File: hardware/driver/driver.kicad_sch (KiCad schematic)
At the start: 71 parts, among them J1 BTB 30P socket, J2 BTB 30P socket, J3 BTB 30P header, J4 BTB 30P header, U1 AT8833CQ, U10 AT8833CQ, U2 AT8833CQ, U3 AT8833CQ, U4 AT8833CQ, U5 AT8833CQ, U6 AT8833CQ, U7 AT8833CQ, U8 AT8833CQ, U9 AT8833CQ

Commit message: Schematic review fixes from datasheet checks
- Crystal: Abracon ABM8-272-T3, which the RP2350 design guide's
  15 pF / 1k values are tuned for (the YXC part needs 20 pF load).
- Status LED: power from V5 and buffer the 3.3 V data through a
  74AHCT1G125; the diode drop left VDD below the 3.7 V minimum.
- Qwiic: drop the BAT54WS power-in path. The ME6211 conducts from
  VOUT to VIN, so a Qwiic-fed 3V3 would back-power V5.
- Notes: sense resistors chop at 0.2-0.29 A rather than fault;
  the NO_ESTOP jumper must be cut when an e-stop is fitted.
- README: AT8833 capacitor values, inductor orientation, VMOT_SENSE
  limits, and open items (V5 capacitance, e-stop masking by a held
  button, E9 reset behaviour on motor inputs).

Co-Authored-By: Claude Opus 5.5 <noreply@anthropic.com>
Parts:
- R1, R10, R11, R12, R13, R14, R15, R16, R17, R18, R19, R2, R20, R3, R4, R5, R6, R7, R8, R9: Note current cap ~0.2-0.29 A; Kelvin return -> chops at 0.2-0.29 A (VTRIP 160-240 mV); Kelvin return
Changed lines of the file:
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@@
 			)
 		)
-		(property "Note" "current cap ~0.2-0.29 A; Kelvin return"
+		(property "Note" "chops at 0.2-0.29 A (VTRIP 160-240 mV); Kelvin return"
 			(at 116.84 40.64 0)
 			(hide yes)
@@
 			)
 		)
-		(property "Note" "current cap ~0.2-0.29 A; Kelvin return"
+		(property "Note" "chops at 0.2-0.29 A (VTRIP 160-240 mV); Kelvin return"
 			(at 167.64 40.64 0)
 			(hide yes)
@@
 			)
 		)
-		(property "Note" "current cap ~0.2-0.29 A; Kelvin return"
+		(property "Note" "chops at 0.2-0.29 A (VTRIP 160-240 mV); Kelvin return"
 			(at 492.76 40.64 0)
 			(hide yes)
@@
 			)
 		)
-		(property "Note" "current cap ~0.2-0.29 A; Kelvin return"
+		(property "Note" "chops at 0.2-0.29 A (VTRIP 160-240 mV); Kelvin return"
 			(at 43.18 86.36 0)
 			(hide yes)
@@
 			)
 		)
-		(property "Note" "current cap ~0.2-0.29 A; Kelvin return"
+		(property "Note" "chops at 0.2-0.29 A (VTRIP 160-240 mV); Kelvin return"
 			(at 368.3 86.36 0)
 			(hide yes)
@@
 			)
 		)
-		(property "Note" "current cap ~0.2-0.29 A; Kelvin return"
+		(property "Note" "chops at 0.2-0.29 A (VTRIP 160-240 mV); Kelvin return"
 			(at 416.56 86.36 0)
 			(hide yes)
@@
 			)
 		)
-		(property "Note" "current cap ~0.2-0.29 A; Kelvin return"
+		(property "Note" "chops at 0.2-0.29 A (VTRIP 160-240 mV); Kelvin return"
 			(at 218.44 129.54 0)
 			(hide yes)
@@
 			)
 		)
-		(property "Note" "current cap ~0.2-0.29 A; Kelvin return"
+		(property "Note" "chops at 0.2-0.29 A (VTRIP 160-240 mV); Kelvin return"
 			(at 266.7 129.54 0)
 			(hide yes)
@@
 			)
 		)
-		(property "Note" "current cap ~0.2-0.29 A; Kelvin return"
+		(property "Note" "chops at 0.2-0.29 A (VTRIP 160-240 mV); Kelvin return"
 			(at 116.84 175.26 0)
 			(hide yes)
@@
 			)
 		)
-		(property "Note" "current cap ~0.2-0.29 A; Kelvin return"
+		(property "Note" "chops at 0.2-0.29 A (VTRIP 160-240 mV); Kelvin return"
 			(at 167.64 175.26 0)
 			(hide yes)
@@
 			)
 		)
-		(property "Note" "current cap ~0.2-0.29 A; Kelvin return"
+		(property "Note" "chops at 0.2-0.29 A (VTRIP 160-240 mV); Kelvin return"
 			(at 492.76 175.26 0)
 			(hide yes)
@@
 			)
 		)
-		(property "Note" "current cap ~0.2-0.29 A; Kelvin return"
+		(property "Note" "chops at 0.2-0.29 A (VTRIP 160-240 mV); Kelvin return"
 			(at 43.18 220.98 0)
 			(hide yes)
@@
 			)
 		)
-		(property "Note" "current cap ~0.2-0.29 A; Kelvin return"
+		(property "Note" "chops at 0.2-0.29 A (VTRIP 160-240 mV); Kelvin return"
 			(at 368.3 220.98 0)
 			(hide yes)
@@
 			)
 		)
-		(property "Note" "current cap ~0.2-0.29 A; Kelvin return"
+		(property "Note" "chops at 0.2-0.29 A (VTRIP 160-240 mV); Kelvin return"
 			(at 416.56 220.98 0)
 			(hide yes)
@@
 			)
 		)
-		(property "Note" "current cap ~0.2-0.29 A; Kelvin return"
+		(property "Note" "chops at 0.2-0.29 A (VTRIP 160-240 mV); Kelvin return"
 			(at 218.44 264.16 0)
 			(hide yes)
@@
 			)
 		)
-		(property "Note" "current cap ~0.2-0.29 A; Kelvin return"
+		(property "Note" "chops at 0.2-0.29 A (VTRIP 160-240 mV); Kelvin return"
 			(at 266.7 264.16 0)
 			(hide yes)
@@
 			)
 		)
-		(property "Note" "current cap ~0.2-0.29 A; Kelvin return"
+		(property "Note" "chops at 0.2-0.29 A (VTRIP 160-240 mV); Kelvin return"
 			(at 116.84 309.88 0)
 			(hide yes)
@@
 			)
 		)
-		(property "Note" "current cap ~0.2-0.29 A; Kelvin return"
+		(property "Note" "chops at 0.2-0.29 A (VTRIP 160-240 mV); Kelvin return"
 			(at 167.64 309.88 0)
 			(hide yes)
@@
 			)
 		)
-		(property "Note" "current cap ~0.2-0.29 A; Kelvin return"
+		(property "Note" "chops at 0.2-0.29 A (VTRIP 160-240 mV); Kelvin return"
 			(at 492.76 309.88 0)
 			(hide yes)
@@
 			)
 		)
-		(property "Note" "current cap ~0.2-0.29 A; Kelvin return"
+		(property "Note" "chops at 0.2-0.29 A (VTRIP 160-240 mV); Kelvin return"
 			(at 43.18 353.06 0)
 			(hide yes)

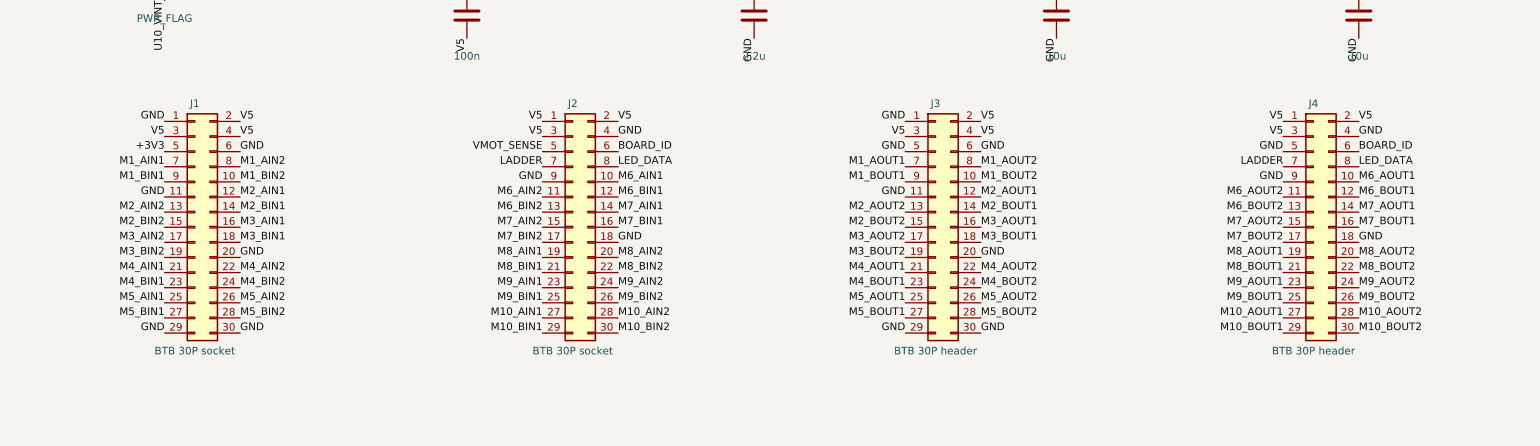
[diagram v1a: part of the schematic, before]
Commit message: Stack: DF40 2.0 mm connectors, 30x30 boards, controller placement
- BTB: Hirose DF40 40-pin, 2.0 mm stack (header DF40C-40DP C424643,
  socket DF40C(2.0)-40DS C597934). The 0.8 mm XUNPU stack left no room
  for parts between boards (the driver QFNs alone are 0.75-0.8 mm).
  Corner contacts are metal fittings per Hirose: tied to GND, not used
  for current. Footprints generated from the catalogue layouts; the
  header's rows are mirrored so pin n mates pin n after the flip.
- Repin: A carries M1-M7, B carries M8-M10 and the utilities, in the
  MCU's pin order so the controller's traces fan in without crossing.
  13 V5 pins across both connectors (was 6).
- Boards grow to 30 x 30 mm; controller is 4-layer, 1.0 mm thick.
- gen/pcbgen.py starts the controller PCB once: outline, stackup,
  JLCPCB rules and net classes, and a first placement of every part
  (buttons over the BTB headers, regulator by its pins, decoupling
  under the MCU). The layout is hand-edited from here.

Co-Authored-By: Claude Opus 5.5 <noreply@anthropic.com>
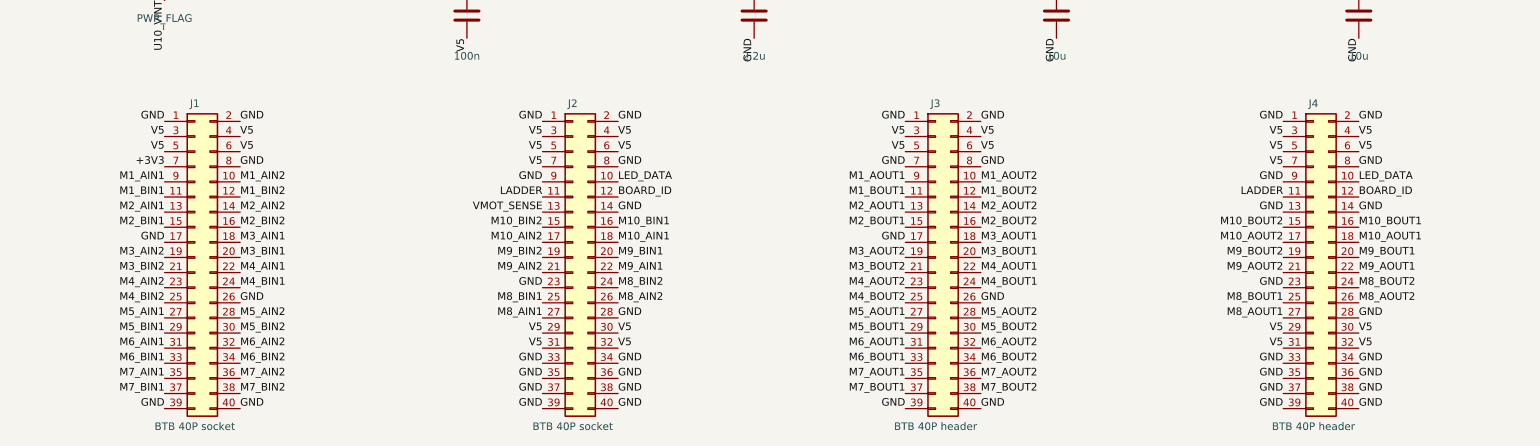
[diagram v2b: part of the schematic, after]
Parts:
- removed J2: BTB 30P socket, stack:XUNPU_BTB0.408-30P_Socket, symbol Connector_Generic:Conn_02x15_Odd_Even
- removed J3, J4: BTB 30P header, stack:XUNPU_BTB0.408-30P_Header, symbol Connector_Generic:Conn_02x15_Odd_Even
- added J2: BTB 40P socket, stack:Hirose_DF40C-2.0-40DS_Socket, symbol Connector_Generic:Conn_02x20_Odd_Even
- added J3, J4: BTB 40P header, stack:Hirose_DF40C-40DP_Header, symbol Connector_Generic:Conn_02x20_Odd_Even
- J1: value BTB 30P socket -> BTB 40P socket; footprint stack:XUNPU_BTB0.408-30P_Socket -> stack:Hirose_DF40C-2.0-40DS_Socket; symbol Connector_Generic:Conn_02x15_Odd_Even -> Connector_Generic:Conn_02x20_Odd_Even; LCSC C42420584 -> C597934; MPN BTB0.408-30PLBDR-M41 -> DF40C(2.0)-40DS-0.4V(51)
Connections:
- net +3V3: now also J1.7 (Pin_7); no longer J1.5 (Pin_5)
- net BOARD_ID: now also J2.12 (Pin_12), J4.12 (Pin_12)
- net GND: now also J1.17 (Pin_17), J1.2 (Pin_2), J1.26 (Pin_26), J1.39 (Pin_39), J1.40 (Pin_40), J1.8 (Pin_8), J2.1 (Pin_1), J2.14 (Pin_14), J2.2 (Pin_2), J2.23 (Pin_23), J2.28 (Pin_28), J2.33 (Pin_33), J2.34 (Pin_34), J2.35 (Pin_35), J2.36 (Pin_36), J2.37 (Pin_37), J2.38 (Pin_38), J2.39 (Pin_39), J2.40 (Pin_40), J2.8 (Pin_8), J2.9 (Pin_9), J3.1 (Pin_1), J3.17 (Pin_17), J3.2 (Pin_2), J3.26 (Pin_26), J3.39 (Pin_39), J3.40 (Pin_40), J3.7 (Pin_7), J3.8 (Pin_8), J4.1 (Pin_1), J4.13 (Pin_13), J4.14 (Pin_14), J4.2 (Pin_2), J4.23 (Pin_23), J4.28 (Pin_28), J4.33 (Pin_33), J4.34 (Pin_34), J4.35 (Pin_35), J4.36 (Pin_36), J4.37 (Pin_37), J4.38 (Pin_38), J4.39 (Pin_39), J4.40 (Pin_40), J4.8 (Pin_8), J4.9 (Pin_9); no longer J1.11 (Pin_11), J1.20 (Pin_20), J1.29 (Pin_29), J1.30 (Pin_30), J1.6 (Pin_6)
- net LADDER: now also J2.11 (Pin_11), J4.11 (Pin_11)
- net LED_DATA: now also J2.10 (Pin_10), J4.10 (Pin_10)
- net M10_AIN1: now also J2.18 (Pin_18)
- net M10_AIN2: now also J2.17 (Pin_17)
- net M10_AOUT1: now also J4.18 (Pin_18)
- net M10_AOUT2: now also J4.17 (Pin_17)
- net M10_BIN1: now also J2.16 (Pin_16)
- net M10_BIN2: now also J2.15 (Pin_15)
- net M10_BOUT1: now also J4.16 (Pin_16)
- net M10_BOUT2: now also J4.15 (Pin_15)
- net M1_AIN1: now also J1.9 (Pin_9); no longer J1.7 (Pin_7)
- net M1_AIN2: now also J1.10 (Pin_10); no longer J1.8 (Pin_8)
- net M1_AOUT1: now also J3.9 (Pin_9)
- net M1_AOUT2: now also J3.10 (Pin_10)
- net M1_BIN1: now also J1.11 (Pin_11); no longer J1.9 (Pin_9)
- net M1_BIN2: now also J1.12 (Pin_12); no longer J1.10 (Pin_10)
- net M1_BOUT1: now also J3.11 (Pin_11)
- net M1_BOUT2: now also J3.12 (Pin_12)
- net M2_AIN1: now also J1.13 (Pin_13); no longer J1.12 (Pin_12)
- net M2_AIN2: now also J1.14 (Pin_14); no longer J1.13 (Pin_13)
- net M2_AOUT1: now also J3.13 (Pin_13)
- net M2_AOUT2: now also J3.14 (Pin_14)
- net M2_BIN1: now also J1.15 (Pin_15); no longer J1.14 (Pin_14)
- net M2_BIN2: now also J1.16 (Pin_16); no longer J1.15 (Pin_15)
- net M2_BOUT1: now also J3.15 (Pin_15)
- net M2_BOUT2: now also J3.16 (Pin_16)
- net M3_AIN1: now also J1.18 (Pin_18); no longer J1.16 (Pin_16)
- net M3_AIN2: now also J1.19 (Pin_19); no longer J1.17 (Pin_17)
- net M3_AOUT1: now also J3.18 (Pin_18)
- net M3_AOUT2: now also J3.19 (Pin_19)
- net M3_BIN1: now also J1.20 (Pin_20); no longer J1.18 (Pin_18)
- net M3_BIN2: now also J1.21 (Pin_21); no longer J1.19 (Pin_19)
- net M3_BOUT1: now also J3.20 (Pin_20)
- net M3_BOUT2: now also J3.21 (Pin_21)
- net M4_AIN1: now also J1.22 (Pin_22); no longer J1.21 (Pin_21)
- net M4_AIN2: now also J1.23 (Pin_23); no longer J1.22 (Pin_22)
- net M4_AOUT1: now also J3.22 (Pin_22)
- net M4_AOUT2: now also J3.23 (Pin_23)
- net M4_BIN1: now also J1.24 (Pin_24); no longer J1.23 (Pin_23)
- net M4_BIN2: now also J1.25 (Pin_25); no longer J1.24 (Pin_24)
- net M4_BOUT1: now also J3.24 (Pin_24)
- net M4_BOUT2: now also J3.25 (Pin_25)
- net M5_AIN1: now also J1.27 (Pin_27); no longer J1.25 (Pin_25)
- net M5_AIN2: now also J1.28 (Pin_28); no longer J1.26 (Pin_26)
- net M5_AOUT1: now also J3.27 (Pin_27)
- net M5_AOUT2: now also J3.28 (Pin_28)
- net M5_BIN1: now also J1.29 (Pin_29); no longer J1.27 (Pin_27)
- net M5_BIN2: now also J1.30 (Pin_30); no longer J1.28 (Pin_28)
- net M5_BOUT1: now also J3.29 (Pin_29)
- net M5_BOUT2: now also J3.30 (Pin_30)
- net M6_AIN1: now also J1.31 (Pin_31)
- net M6_AIN2: now also J1.32 (Pin_32)
- net M6_AOUT1: now also J3.31 (Pin_31)
- net M6_AOUT2: now also J3.32 (Pin_32)
- net M6_BIN1: now also J1.33 (Pin_33)
- net M6_BIN2: now also J1.34 (Pin_34)
- net M6_BOUT1: now also J3.33 (Pin_33)
- net M6_BOUT2: now also J3.34 (Pin_34)
- net M7_AIN1: now also J1.35 (Pin_35)
- net M7_AIN2: now also J1.36 (Pin_36)
- net M7_AOUT1: now also J3.35 (Pin_35)
- net M7_AOUT2: now also J3.36 (Pin_36)
- net M7_BIN1: now also J1.37 (Pin_37)
- net M7_BIN2: now also J1.38 (Pin_38)
- net M7_BOUT1: now also J3.37 (Pin_37)
- net M7_BOUT2: now also J3.38 (Pin_38)
- net M8_AIN1: now also J2.27 (Pin_27)
- net M8_AIN2: now also J2.26 (Pin_26)
- net M8_AOUT1: now also J4.27 (Pin_27)
- net M8_AOUT2: now also J4.26 (Pin_26)
- net M8_BIN1: now also J2.25 (Pin_25)
- net M8_BIN2: now also J2.24 (Pin_24)
- net M8_BOUT1: now also J4.25 (Pin_25)
- net M8_BOUT2: now also J4.24 (Pin_24)
- net M9_AIN1: now also J2.22 (Pin_22)
- net M9_AIN2: now also J2.21 (Pin_21)
- net M9_AOUT1: now also J4.22 (Pin_22)
- net M9_AOUT2: now also J4.21 (Pin_21)
- net M9_BIN1: now also J2.20 (Pin_20)
- net M9_BIN2: now also J2.19 (Pin_19)
- net M9_BOUT1: now also J4.20 (Pin_20)
- net M9_BOUT2: now also J4.19 (Pin_19)
- net V5: now also J1.5 (Pin_5), J1.6 (Pin_6), J2.29 (Pin_29), J2.3 (Pin_3), J2.30 (Pin_30), J2.31 (Pin_31), J2.32 (Pin_32), J2.4 (Pin_4), J2.5 (Pin_5), J2.6 (Pin_6), J2.7 (Pin_7), J3.3 (Pin_3), J3.4 (Pin_4), J3.5 (Pin_5), J3.6 (Pin_6), J4.29 (Pin_29), J4.3 (Pin_3), J4.30 (Pin_30), J4.31 (Pin_31), J4.32 (Pin_32), J4.4 (Pin_4), J4.5 (Pin_5), J4.6 (Pin_6), J4.7 (Pin_7); no longer J1.2 (Pin_2)
- net VMOT_SENSE: now also J2.13 (Pin_13)

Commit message: Controller: fully routed
- BTN1/BTN2 -> XUNPU TS-1088-AR02016 (C720477), stacked in the top-right
  corner with R11/R12 under them: the TS-1187A pads over the BTB headers
  blocked the connector fan-out.
- Connector B moved 2 mm down (stack still keyed by A's +2 mm offset);
  ladder/board-ID resistor column moved right, out of the M8 path.
- BTB corner contacts left unconnected (Hirose metal fittings).
- Routing: Freerouting 2.5.0 for the bulk, then a small grid router for
  the remaining nets and plane stitching. DRC: 0 unconnected, only
  silkscreen warnings and one harmless track stub left.

Co-Authored-By: Claude Opus 5.5 <noreply@anthropic.com>
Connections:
- net GND: no longer J1.1 (Pin_1), J1.2 (Pin_2), J1.39 (Pin_39), J1.40 (Pin_40), J2.1 (Pin_1), J2.2 (Pin_2), J2.39 (Pin_39), J2.40 (Pin_40), J3.1 (Pin_1), J3.2 (Pin_2), J3.39 (Pin_39), J3.40 (Pin_40), J4.1 (Pin_1), J4.2 (Pin_2), J4.39 (Pin_39), J4.40 (Pin_40)
- no-connect marks 0 -> 16
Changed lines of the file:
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@@
 		)
 	)
-	(label "GND"
-		(at 142.24 370.84 180)
-		(effects
-			(font
-				(size 1.27 1.27)
-			)
-			(justify right bottom)
-		)
-	)
-	(label "GND"
-		(at 154.94 370.84 0)
-		(effects
-			(font
-				(size 1.27 1.27)
-			)
-			(justify left bottom)
-		)
+	(no_connect
+		(at 142.24 370.84)
+	)
+	(no_connect
+		(at 154.94 370.84)
 	)
 	(label "V5"
@@
 		)
 	)
-	(label "GND"
-		(at 142.24 419.1 180)
-		(effects
-			(font
-				(size 1.27 1.27)
-			)
-			(justify right bottom)
-		)
-	)
-	(label "GND"
-		(at 154.94 419.1 0)
-		(effects
-			(font
-				(size 1.27 1.27)
-			)
-			(justify left bottom)
-		)
+	(no_connect
+		(at 142.24 419.1)
+	)
+	(no_connect
+		(at 154.94 419.1)
 	)
 	(symbol
@@
 		)
 	)
-	(label "GND"
-		(at 205.74 370.84 180)
-		(effects
-			(font
-				(size 1.27 1.27)
-			)
-			(justify right bottom)
-		)
-	)
-	(label "GND"
-		(at 218.44 370.84 0)
-		(effects
-			(font
-				(size 1.27 1.27)
-			)
-			(justify left bottom)
-		)
+	(no_connect
+		(at 205.74 370.84)
+	)
+	(no_connect
+		(at 218.44 370.84)
 	)
 	(label "V5"
@@
 		)
 	)
-	(label "GND"
-		(at 205.74 419.1 180)
-		(effects
-			(font
-				(size 1.27 1.27)
-			)
-			(justify right bottom)
-		)
-	)
-	(label "GND"
-		(at 218.44 419.1 0)
-		(effects
-			(font
-				(size 1.27 1.27)
-			)
-			(justify left bottom)
-		)
+	(no_connect
+		(at 205.74 419.1)
+	)
+	(no_connect
+		(at 218.44 419.1)
 	)
 	(symbol
@@
 		)
 	)
-	(label "GND"
-		(at 266.7 370.84 180)
-		(effects
-			(font
-				(size 1.27 1.27)
-			)
-			(justify right bottom)
-		)
-	)
-	(label "GND"
-		(at 279.4 370.84 0)
-		(effects
-			(font
-				(size 1.27 1.27)
-			)
-			(justify left bottom)
-		)
+	(no_connect
+		(at 266.7 370.84)
+	)
+	(no_connect
+		(at 279.4 370.84)
 	)
 	(label "V5"
@@
 		)
 	)
-	(label "GND"
-		(at 266.7 419.1 180)
-		(effects
-			(font
-				(size 1.27 1.27)
-			)
-			(justify right bottom)
-		)
-	)
-	(label "GND"
-		(at 279.4 419.1 0)
-		(effects
-			(font
-				(size 1.27 1.27)
-			)
-			(justify left bottom)
-		)
+	(no_connect
+		(at 266.7 419.1)
+	)
+	(no_connect
+		(at 279.4 419.1)
 	)
 	(symbol
@@
 		)
 	)
-	(label "GND"
-		(at 330.2 370.84 180)
-		(effects
-			(font
-				(size 1.27 1.27)
-			)
-			(justify right bottom)
-		)
-	)
-	(label "GND"
-		(at 342.9 370.84 0)
-		(effects
-			(font
-				(size 1.27 1.27)
-			)
-			(justify left bottom)
-		)
+	(no_connect
+		(at 330.2 370.84)
+	)
+	(no_connect
+		(at 342.9 370.84)
 	)
 	(label "V5"
@@
 		)
 	)
-	(label "GND"
-		(at 330.2 419.1 180)
-		(effects
-			(font
-				(size 1.27 1.27)
-			)
-			(justify right bottom)
-		)
-	)
-	(label "GND"
-		(at 342.9 419.1 0)
-		(effects
-			(font
-				(size 1.27 1.27)
-			)
-			(justify left bottom)
-		)
+	(no_connect
+		(at 330.2 419.1)
+	)
+	(no_connect
+		(at 342.9 419.1)
 	)
 	(symbol

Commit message: single_sh: routed single-board PCB; BOM scrub
New single-board versions of the circuit (controller + driver + IO variant
on one PCB, BTBs removed): single_sh and single_xh schematics from single()
in gen/build.py. single_sh also gets a routed board:

- 122 x 20 mm, 4 layers, 1.6 mm, all parts on top. In1 GND; In2 V5 with a
  3V3 island under the MCU (thin finger to the LDO); F/B signals.
- Along the board: USB-C + power | drivers M4-M1 | MCU | drivers M10-M5 |
  LED strip. Motor connectors J12 J11 | J15 J14 J13 so each bus leaves the
  MCU in pin order; misc connectors along the other long edge.
- Driver cells pre-routed (A1/A2 cross B1/B2 on In2 jumpers), core
  regulator copied from the controller, rest Freerouting 2.5.0 + a small
  grid router. V5 via clusters at the FET, ext-5V diode and strip fuse.
- DRC: 0 errors, 0 unconnected, schematic parity clean; 24 silkscreen
  warnings (footprint outlines).
- gen/pcbgen.py: build() split out of main(), per-board size/thickness,
  polygon zones, single_sh() placement (reproduces the routed board).

BOOTSEL on the single boards is now the TS-1088-AR02016 (C720477), same as
BTN1/BTN2; the stacked controller keeps its TS-1187A.

BOM scrub (all boards; numbers checked against the JLCPCB library):
- Every passive gets LCSC/MPN (PASSIVES in gen/build.py), basic where one
  exists. VM caps now 16 V (basic 2.2 uF is 6.3 V).
- Polyfuse C702823 (not in JLCPCB's library) -> C209721, same rating.
- Status LED C965555 (1 in stock) -> XL-2020RGBC-WS2812B C5349955, same
  pinout and footprint.
- J8 B3B-PH-K-S gets C131339.
- Solder jumpers and test pads excluded from BOM and placement files
  (schgen in_bom support; pcbgen follows the symbol).
- Schematics and *_bom.csv regenerated; controller PCB fields/attributes
  synced (layout unchanged).

Co-Authored-By: Claude Opus 5.5 <noreply@anthropic.com>
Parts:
- C1, C10, C13, C16, C19, C22, C25, C28, C4, C7: LCSC (none) -> C52923; MPN (none) -> CL05A105KA5NQNC
- C11, C14, C17, C2, C20, C23, C26, C29, C34, C5, C8: LCSC (none) -> C1525; MPN (none) -> CL05B104KO5NNNC
- C12, C15, C18, C21, C24, C27, C3, C30, C6, C9: LCSC (none) -> C170151; MPN (none) -> CL05A225KO5NQNC
- C31, C32, C33: LCSC (none) -> C15850; MPN (none) -> CL21A106KAYNNNE
- R1, R10, R11, R12, R13, R14, R15, R16, R17, R18, R19, R2, R20, R3, R4, R5, R6, R7, R8, R9: LCSC (none) -> C728435; MPN (none) -> RL0402FR-070R82L
- R21: LCSC (none) -> C25792; MPN (none) -> 0402WGF4702TCE
- R22: LCSC (none) -> C25783; MPN (none) -> 0402WGF3902TCE
- R23: LCSC (none) -> C25744; MPN (none) -> 0402WGF1002TCE
